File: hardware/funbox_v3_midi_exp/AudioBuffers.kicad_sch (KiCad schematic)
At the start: 35 parts, among them U1 TL074

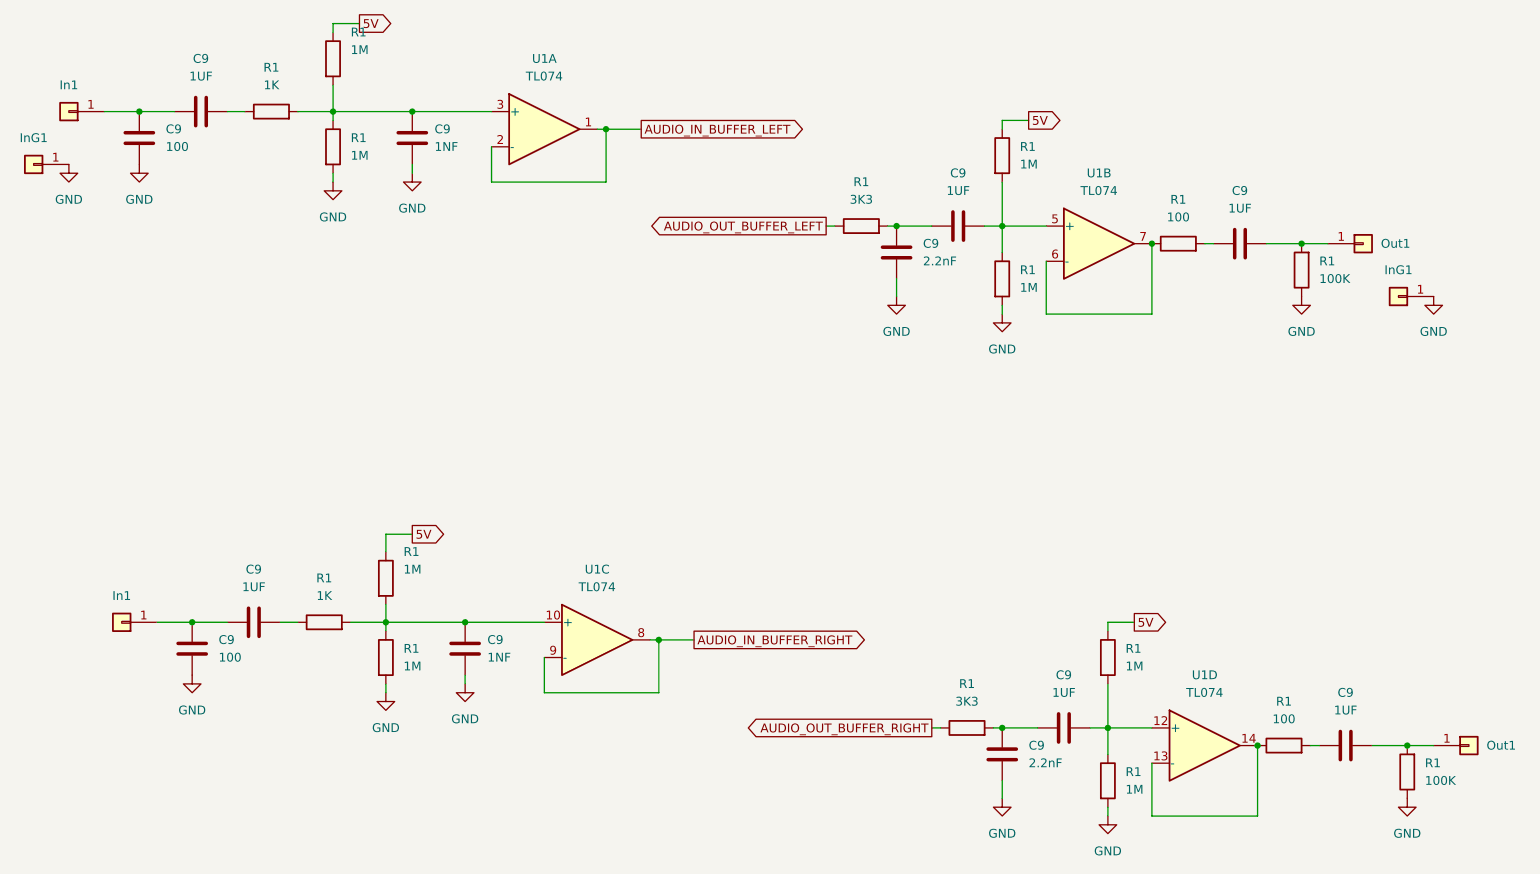
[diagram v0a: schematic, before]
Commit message: Updated schematic with new quad op amp
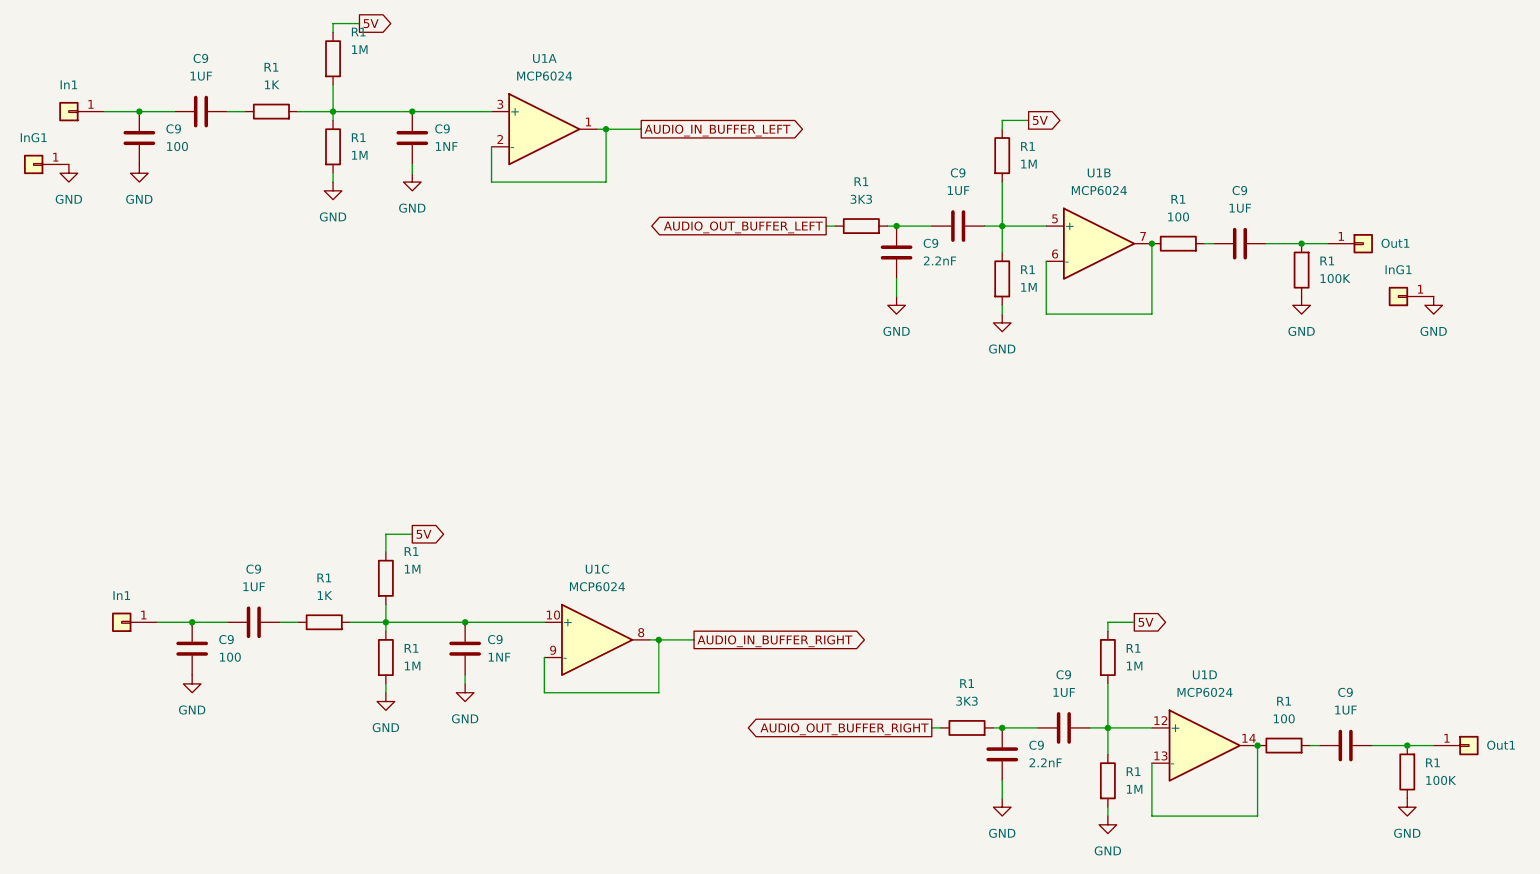
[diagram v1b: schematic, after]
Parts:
- U1: value TL074 -> MCP6024
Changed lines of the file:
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@@
       (effects (font (size 1.27 1.27)))
     )
-    (property "Value" "TL074" (at 113.03 39.37 0)
+    (property "Value" "MCP6024" (at 113.03 39.37 0)
       (effects (font (size 1.27 1.27)))
     )
@@
       (effects (font (size 1.27 1.27)))
     )
-    (property "Value" "TL074" (at 120.65 113.03 0)
+    (property "Value" "MCP6024" (at 120.65 113.03 0)
       (effects (font (size 1.27 1.27)))
     )
@@
       (effects (font (size 1.27 1.27)))
     )
-    (property "Value" "TL074" (at 193.04 55.88 0)
+    (property "Value" "MCP6024" (at 193.04 55.88 0)
       (effects (font (size 1.27 1.27)))
     )
@@
       (effects (font (size 1.27 1.27)))
     )
-    (property "Value" "TL074" (at 208.28 128.27 0)
-      (effects (font (size 1.27 1.27)))
-    )
+    (property "Value" "MCP6024" (at 208.28 128.27 0)
+      (effects (font (size 1.27 1.27)))
+    )
